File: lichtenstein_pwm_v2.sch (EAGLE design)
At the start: 90 parts, among them IC1 MAX11647, IC2 MCP23017, IC3 74AHCT125SOIC14, IC5 LM75B, IC9 LD1117, J1 MAGJACK, U1 ONION-OMEGA2

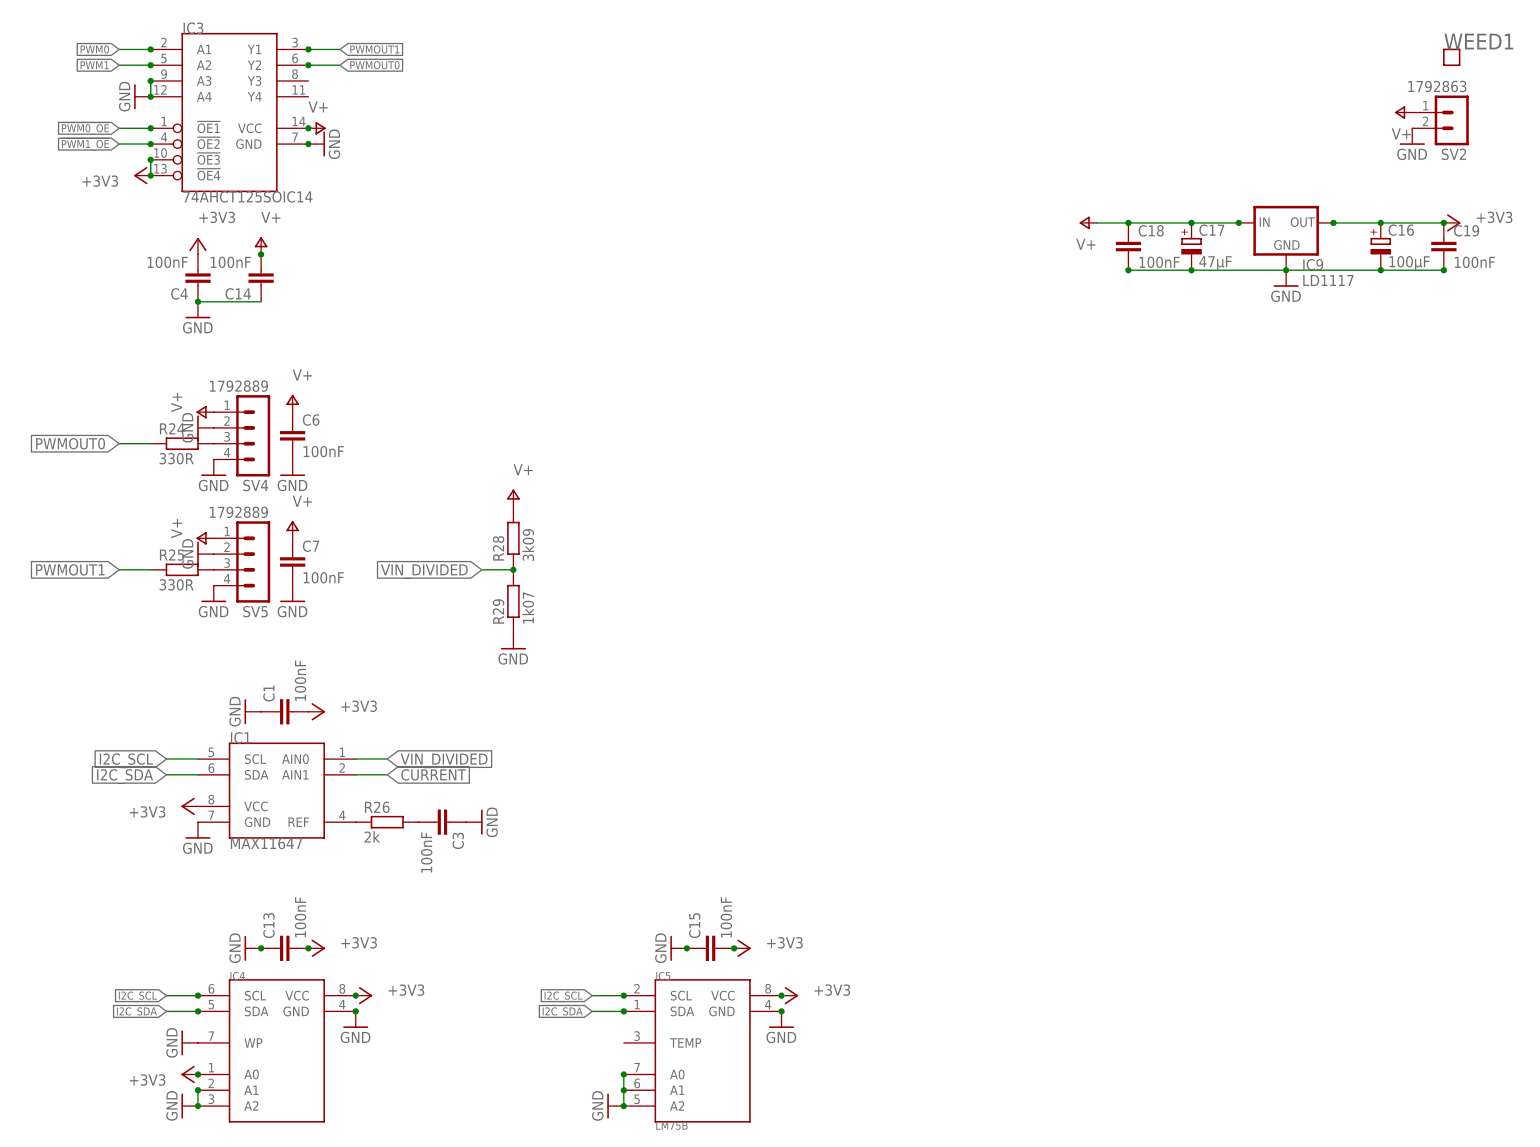
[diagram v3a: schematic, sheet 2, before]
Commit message: added current sense amplifier; replaced footprints of some large resevoir caps
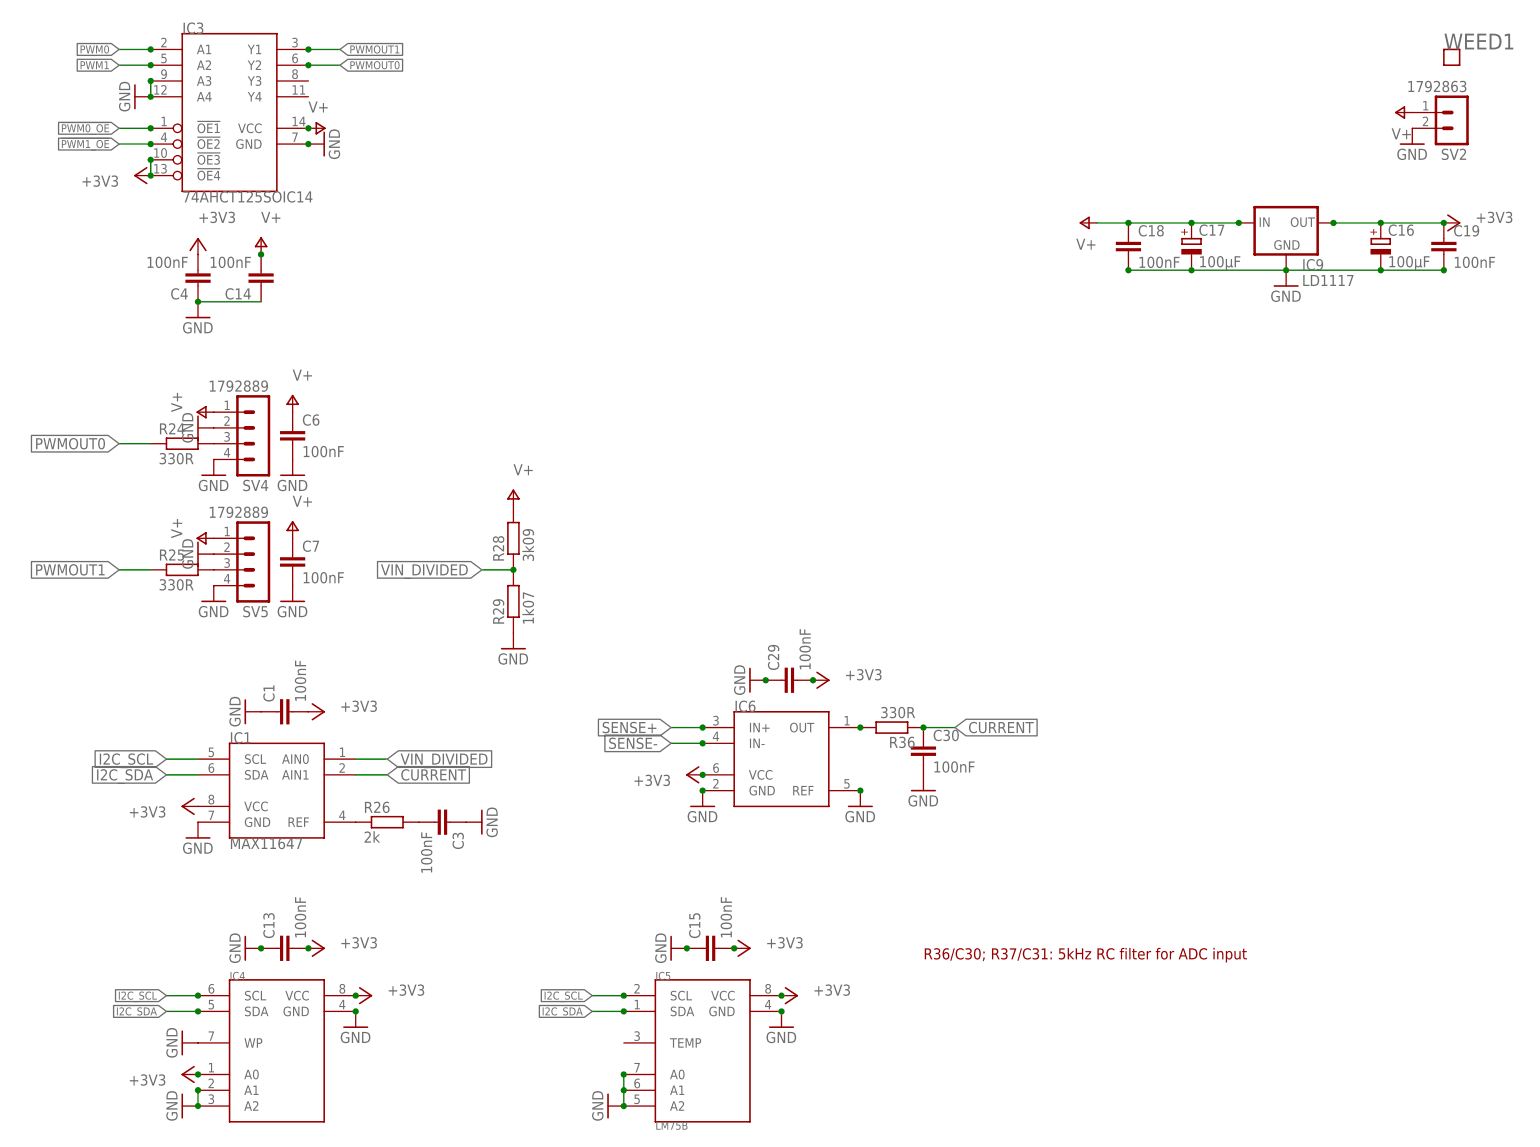
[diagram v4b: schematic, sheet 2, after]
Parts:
- added C29, C30: 100nF, rcl:C-EUC0805
- added IC6: (no value), lichtenstein_onion:INA18120VVSOT-23
- added R36: 330R, rcl:R-EU_M0805
- C17: value 47µF -> 100µF; device rcl:CPOL-EUCT7343 -> rcl:CPOL-EUD; MOUSER 581-TAJD476M016RNJV -> 667-EEE-HC1C101XP
- C5: device rcl:CPOL-EUCT7343 -> rcl:CPOL-EUSMCC; MOUSER 581-TAJD476M016RNJV -> 581-TAJC476K016SNJ
- C9: device rcl:CPOL-EUSMCD -> rcl:CPOL-EUSMCC; MOUSER 581-TAJD476M016RNJV -> 581-TAJC476K016SNJ
- R24, R25: MOUSER (none) -> 71-CRCW0805330RFKEAC
- R26: MOUSER (none) -> 667-ERJ-6ENF2001V
- R28: MOUSER (none) -> 652-CR0805FX-3091ELF
- R29: MOUSER (none) -> 652-CR0805FX-1071ELF
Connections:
- new net N$21: IC6.OUT, R36.2
- new net SENSE+: IC6.IN+
- new net SENSE-: IC6.IN-
- net +3V3: now also C29.2, IC6.VCC
- net CURRENT: now also C30.1, R36.1
- net GND: now also C29.1, C30.2, IC6.GND, IC6.REF
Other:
- note added: "R36/C30; R37/C31: 5kHz RC filter for ADC input"

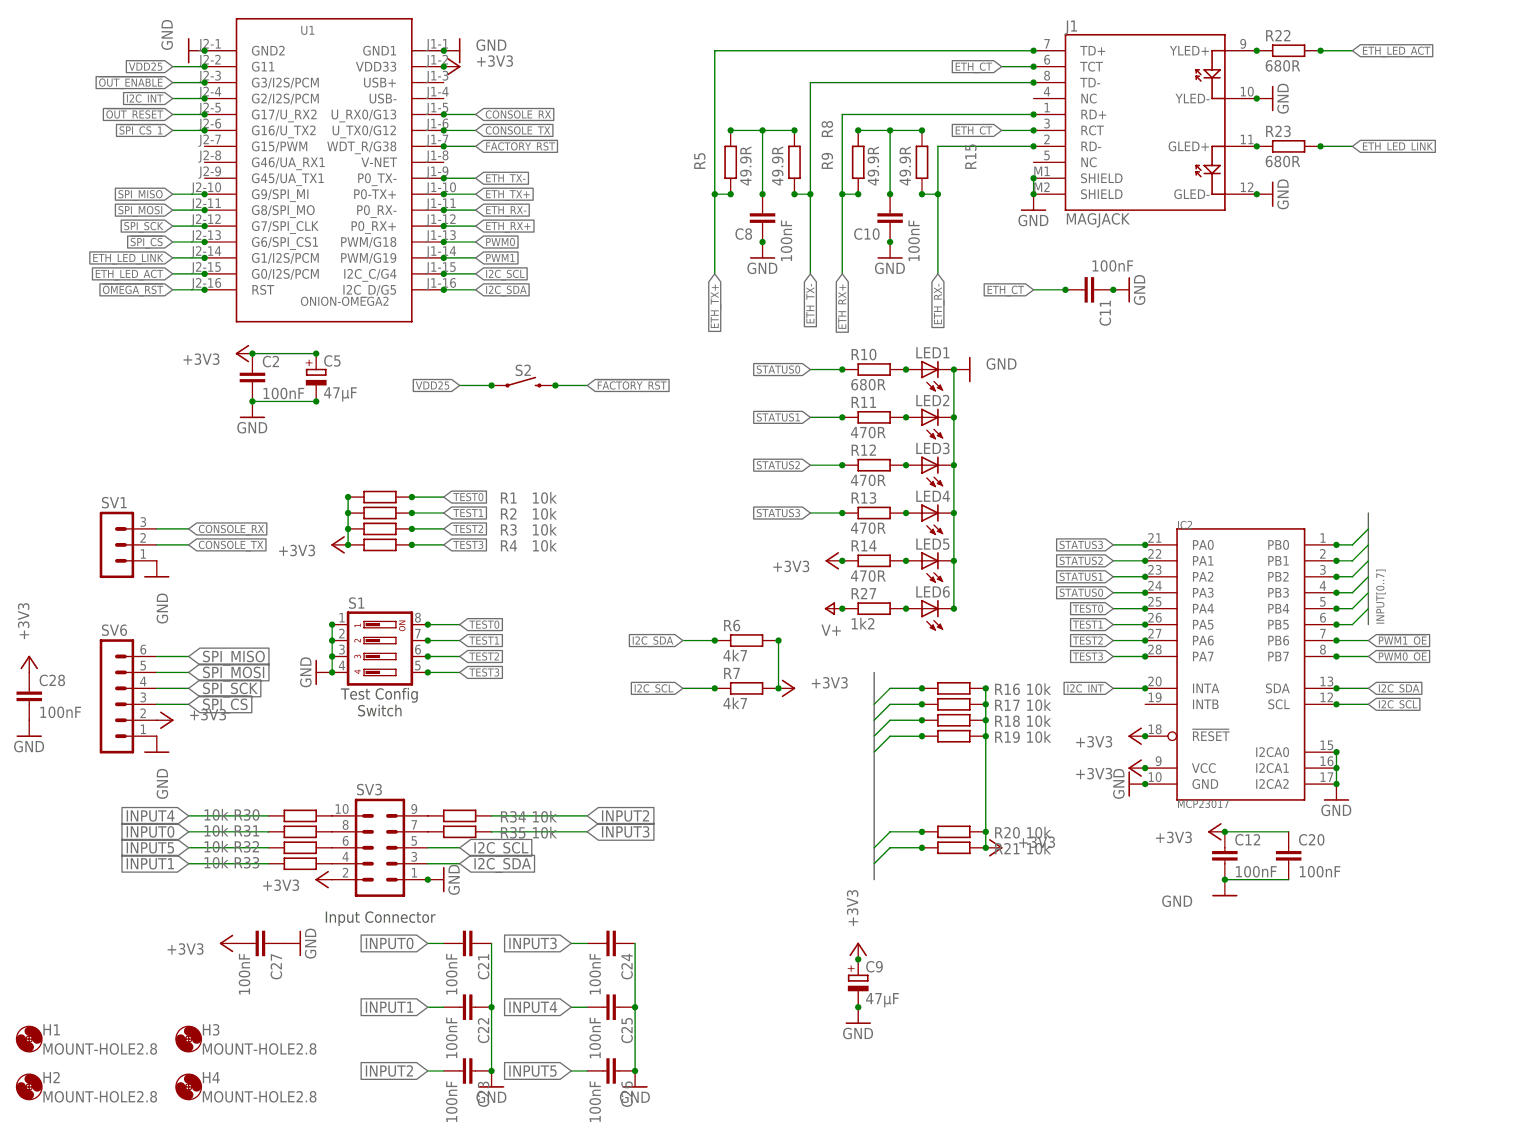
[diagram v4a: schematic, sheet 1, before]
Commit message: removed input connector, cleaned up some signals
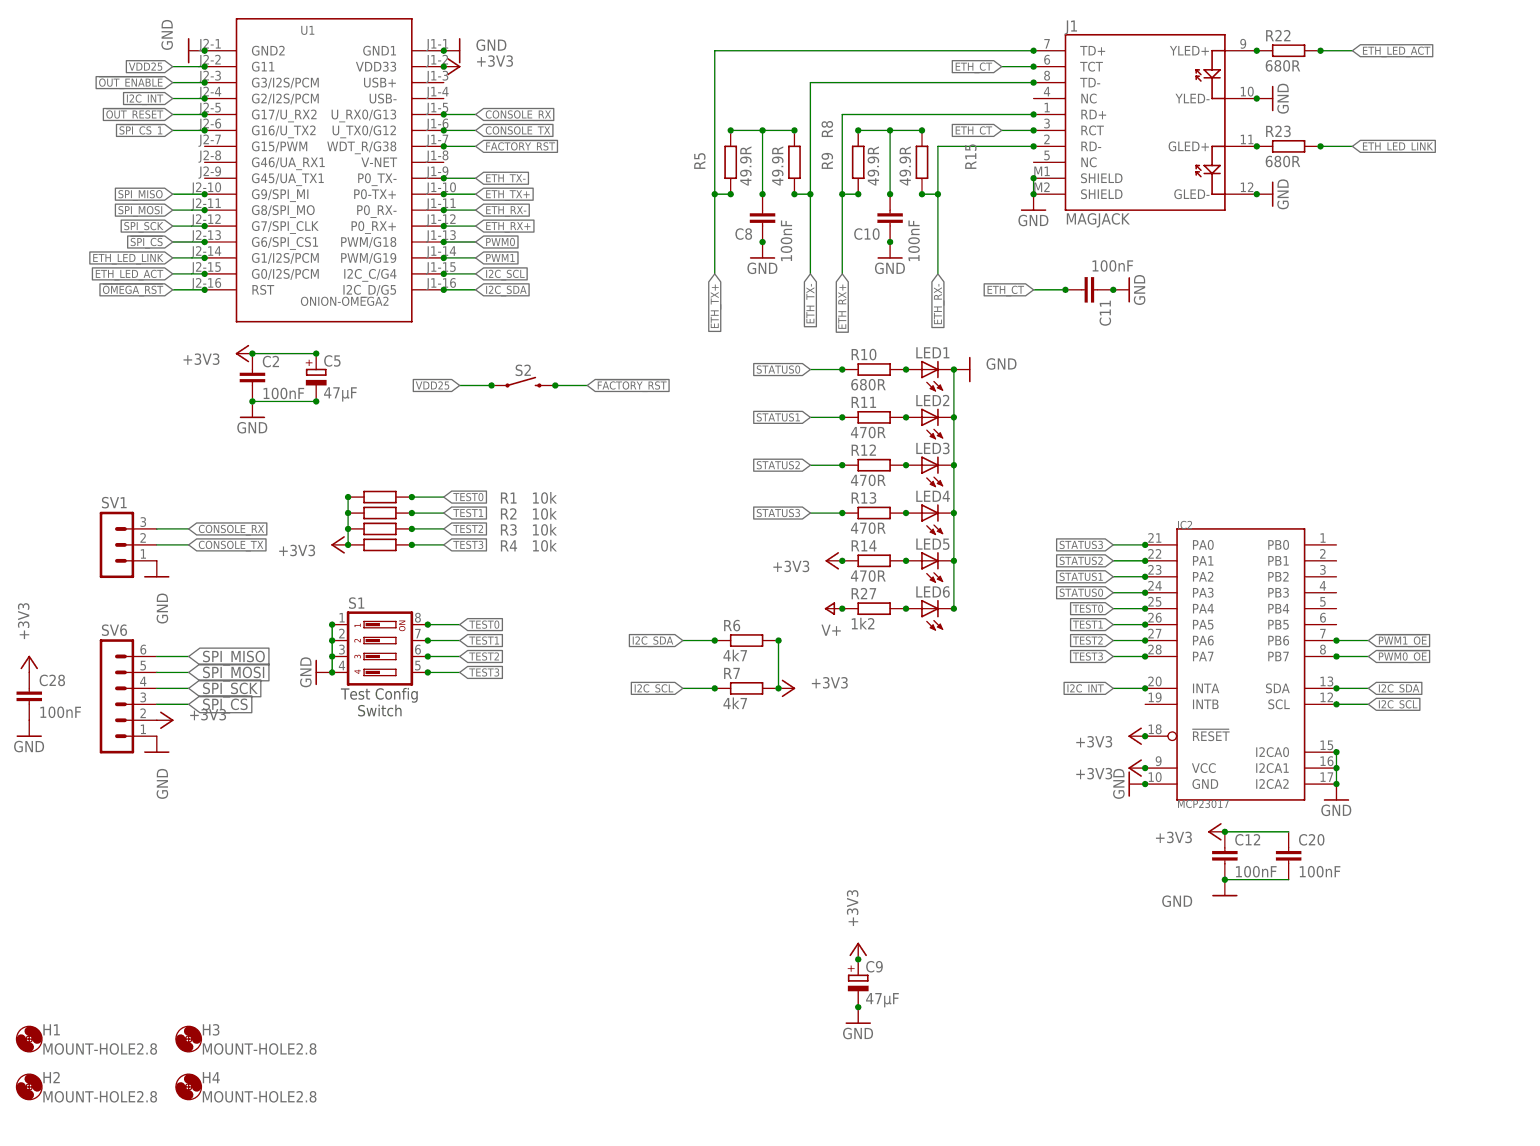
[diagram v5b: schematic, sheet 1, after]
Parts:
- removed C21, C22, C23, C24, C25, C26, C27: 100nF, rcl:C-EUC0805
- removed R16, R17, R18, R19, R20, R21, R30, R31, R32, R33, R34, R35: 10k, rcl:R-EU_M0805
- removed SV3: (no value), con-lstb:MA05-2
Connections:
- removed net INPUT0: C21.2, IC2.PB1, R16.1, R31.2
- removed net INPUT1: C22.2, IC2.PB3, R17.1, R33.2
- removed net INPUT2: C23.2, IC2.PB5, R20.1, R34.2
- removed net INPUT3: C24.2, IC2.PB4, R21.1, R35.2
- removed net INPUT4: C25.2, IC2.PB0, R18.1, R30.2
- removed net INPUT5: C26.2, IC2.PB2, R19.1, R32.2
- removed net N$15: R30.1, SV3.10
- removed net N$16: R31.1, SV3.8
- removed net N$17: R32.1, SV3.6
- removed net N$18: R33.1, SV3.4
- removed net N$19: R34.1, SV3.9
- removed net N$20: R35.1, SV3.7
- net +3V3: no longer C27.2, IC4.A0, R16.2, R17.2, R18.2, R19.2, R20.2, R21.2, SV3.2
- net GND: now also IC4.A0; no longer C21.1, C22.1, C23.1, C24.1, C25.1, C26.1, C27.1, SV3.1
- net I2C_SCL: no longer SV3.5
- net I2C_SDA: no longer SV3.3
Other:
- note removed: "Input Connector"

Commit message: more board clean-up
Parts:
- removed C28, C29, C30: 100nF, rcl:C-EUC0805
- removed R27: 1k2, rcl:R-EU_M0805
- removed R28: 3k09, rcl:R-EU_M0805
- removed R29: 1k07, rcl:R-EU_M0805
- removed R36: 330R, rcl:R-EU_M0805
- added C21, C24: 100nF, rcl:C-EUC0805
- added C22: 100µF, rcl:CPOL-EUD
- added C23: 100µF, rcl:CPOL-EUCT7343
- added R16: 49.9R, rcl:R-EU_M0805
- added R17, R18: 680R, rcl:R-EU_M0805
- added R19: 330R, rcl:R-EU_M0805
- added SV3: (no value), con-lstb:MA04-1
- C16: value 100µF -> 100nF; device rcl:CPOL-EUCT7343 -> rcl:C-EUC0805; MOUSER 581-NOSD107M006 -> 710-885012207072
- C17: value 100µF -> 100nF; device rcl:CPOL-EUD -> rcl:C-EUC0805; MOUSER 667-EEE-HC1C101XP -> 710-885012207072
- C4, C6: value 100nF -> 47µF; device rcl:C-EUC0805 -> rcl:CPOL-EUSMCC; MOUSER 710-885012207072 -> 581-TAJC476K016SNJ
- C5, C9: value 47µF -> 100nF; device rcl:CPOL-EUSMCC -> rcl:C-EUC0805; MOUSER 581-TAJC476K016SNJ -> 710-885012207072
- IC1: value MAX11647 -> MCP23017; device lichtenstein_onion:MAX11647UMAX-8 -> lichtenstein_onion:MCP23017SOIC28
- IC2: value MCP23017 -> 74AHCT125SOIC14; device lichtenstein_onion:MCP23017SOIC28 -> lichtenstein_onion:74AHCT125SOIC14
- IC3: value 74AHCT125SOIC14 -> MAX11647; device lichtenstein_onion:74AHCT125SOIC14 -> lichtenstein_onion:MAX11647UMAX-8
- R15: value 49.9R -> 1k2; MOUSER 652-CR0805FX-49R9ELF -> 755-ESR10EZPJ122
- R22: value 680R -> 3k09; MOUSER 652-CR0805-FX6800GLF -> 652-CR0805FX-3091ELF
- R23: value 680R -> 1k07; MOUSER 652-CR0805-FX6800GLF -> 652-CR0805FX-1071ELF
- SV2: value 1792863 -> (none); device lichtenstein_onion:1792863 -> con-lstb:MA06-1
- SV6: value (none) -> 1792863; device con-lstb:MA06-1 -> lichtenstein_onion:1792863
- renumbered IC9 to IC7, R25 to R20, R26 to R21
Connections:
- net !PWM0_OE: now also IC1.PB7, IC2.!OE1; no longer IC2.PB7, IC3.!OE1
- net !PWM1_OE: now also IC1.PB6, IC2.!OE2; no longer IC2.PB6, IC3.!OE2
- net !SPI_CS: now also SV2.3; no longer SV6.3
- net +3V3: now also C1.1, C10.1, C11.2, C14.2, C18.2, C19.2, C23.+, C24.1, C3.1, C4.+, C6.+, C9.1, IC1.!RESET, IC2.!OE3, IC2.!OE4, IC3.VCC, SV2.2, SV3.2; no longer C1.2, C12.1, C15.2, C16.+, C19.1, C20.1, C28.1, C29.2, C4.2, C5.+, C9.+, IC2.!RESET, IC2.VCC, IC3.!OE3, IC3.!OE4, SV6.2
- net CURRENT: now also C20.1, IC3.AIN1, R24.1; no longer C30.1, IC1.AIN1, R36.1
- net ETH_CT: now also C8.2; no longer C11.2
- net ETH_LED_ACT: now also R17.2; no longer R22.2
- net ETH_LED_LINK: now also R18.2; no longer R23.2
- net ETH_RX-: now also R16.1; no longer R15.1
- net GND: now also C1.2, C10.2, C12.1, C15.2, C16.2, C17.1, C18.1, C19.1, C21.2, C22.-, C23.-, C24.2, C3.2, C4.-, C5.1, C6.-, C7.1, C9.2, IC1.I2CA0, IC1.I2CA1, IC1.I2CA2, IC2.A3, IC2.A4, R23.1, SV2.1, SV3.1, SV6.2; no longer C1.1, C10.1, C12.2, C15.1, C16.-, C17.-, C18.2, C19.2, C28.2, C29.1, C3.1, C30.2, C4.1, C5.-, C6.2, C7.2, C9.-, IC2.I2CA0, IC2.I2CA1, IC2.I2CA2, IC3.A3, IC3.A4, R29.1, SV2.2, SV6.1
- net I2C_INT: now also IC1.INTA; no longer IC2.INTA
- net I2C_SCL: now also IC3.SCL, SV3.3; no longer IC2.SCL
- net I2C_SDA: now also IC3.SDA, SV3.4; no longer IC2.SDA
- net N$12: now also IC3.REF; no longer IC1.REF
- net N$13: now also C17.2; no longer C3.2
- net N$14: now also R15.2; no longer R27.2
- net N$21: now also R24.2; no longer R36.2
- net N$3: now also C5.2; no longer C8.2
- net N$4: now also R17.1; no longer R22.1
- net N$5: now also R18.1; no longer R23.1
- net N$6: now also C7.2, R16.2; no longer C10.2, R15.2
- net N$7: now also R19.2; no longer R24.2
- net PWM0: now also IC2.A1; no longer IC3.A1
- net PWM1: now also IC2.A2; no longer IC3.A2
- net PWMOUT0: now also IC2.Y2, R19.1; no longer IC3.Y2, R24.1
- net PWMOUT1: now also IC2.Y1; no longer IC3.Y1
- net SPI_MISO: now also SV2.6; no longer SV6.6
- net SPI_MOSI: now also SV2.5; no longer SV6.5
- net SPI_SCK: now also SV2.4; no longer SV6.4
- net STATUS0: now also IC1.PA3; no longer IC2.PA3
- net STATUS1: now also IC1.PA2; no longer IC2.PA2
- net STATUS2: now also IC1.PA1; no longer IC2.PA1
- net STATUS3: now also IC1.PA0; no longer IC2.PA0
- net TEST0: now also IC1.PA4; no longer IC2.PA4
- net TEST1: now also IC1.PA5; no longer IC2.PA5
- net TEST2: now also IC1.PA6; no longer IC2.PA6
- net TEST3: now also IC1.PA7; no longer IC2.PA7
- net V+: now also C12.2, C15.1, C16.1, C21.1, C22.+, IC2.VCC, R15.1, R22.2, SV6.1; no longer C14.2, C17.+, C18.1, C6.1, C7.1, IC3.VCC, R27.1, R28.2, SV2.1
- net VIN_DIVIDED: now also IC3.AIN0, R22.1, R23.2; no longer IC1.AIN0, R28.1, R29.2
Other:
- moved on the sheet: C10, C13, C14, C15, C18, C19, C2, C8, R15, R24
